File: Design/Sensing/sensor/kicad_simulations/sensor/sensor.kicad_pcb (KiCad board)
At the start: 2 copper layers, 41 parts, among them J1 Conn_01x14_Pin, J10 Conn_01x02_Pin, J11 Conn_01x01_Pin, J12 Conn_01x02_Pin, J13 Conn_01x02_Pin, J14 Conn_01x02_Pin, J15 Conn_01x02_Pin, J16 Conn_01x01_Pin, J17 Conn_01x02_Pin, J2 Conn_01x14_Pin, J3 Conn_01x02_Pin, J4 Conn_01x02_Pin, J5 Conn_01x02_Pin, J6 Conn_01x01_Pin, J7 Conn_01x02_Pin, J8 Conn_01x02_Pin, J9 Conn_01x02_Pin, Q1 2N3904, Q2 2N3904, Q3 2N3904, U1 TSSP58038, U2 TSSP58038, U3 TSSP58038, U4 BUF602xD, U5 BUF602xD, U6 BUF602xD

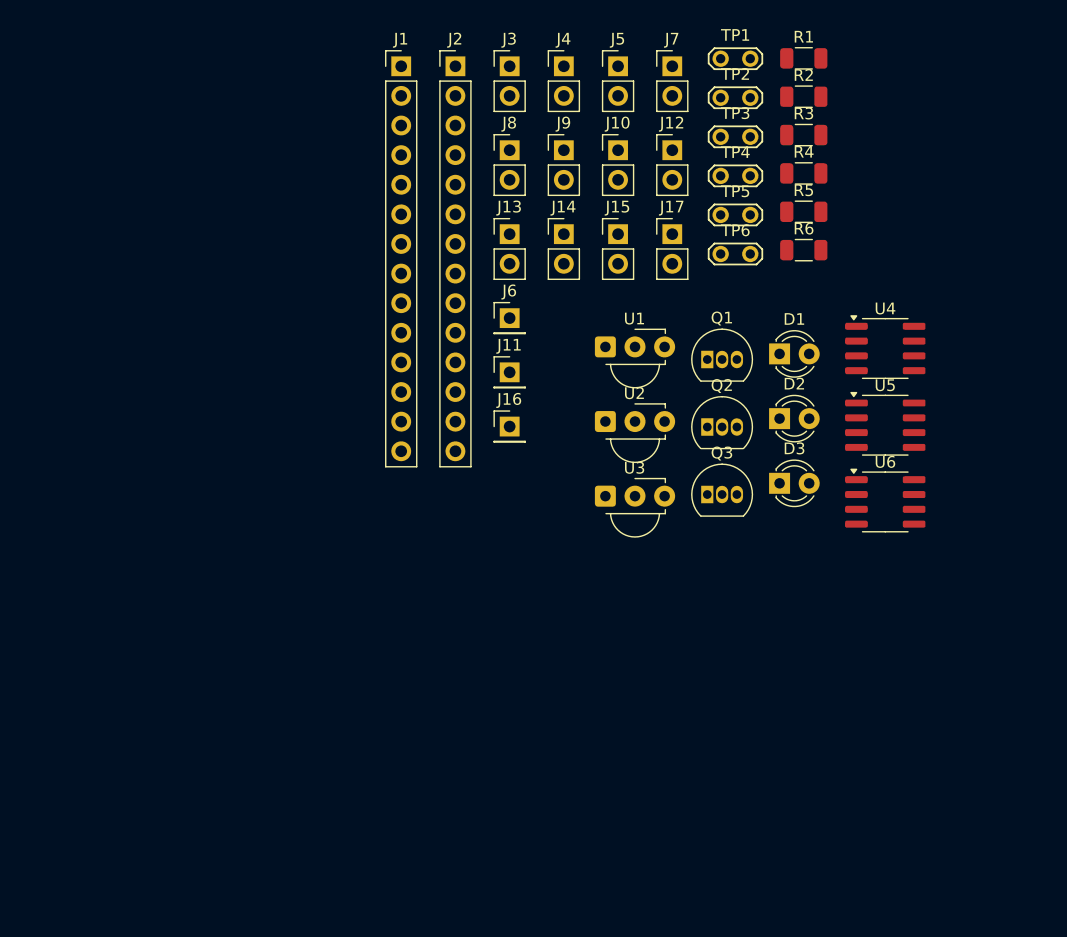
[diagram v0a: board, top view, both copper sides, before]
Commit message: PCB components placed but unrooted
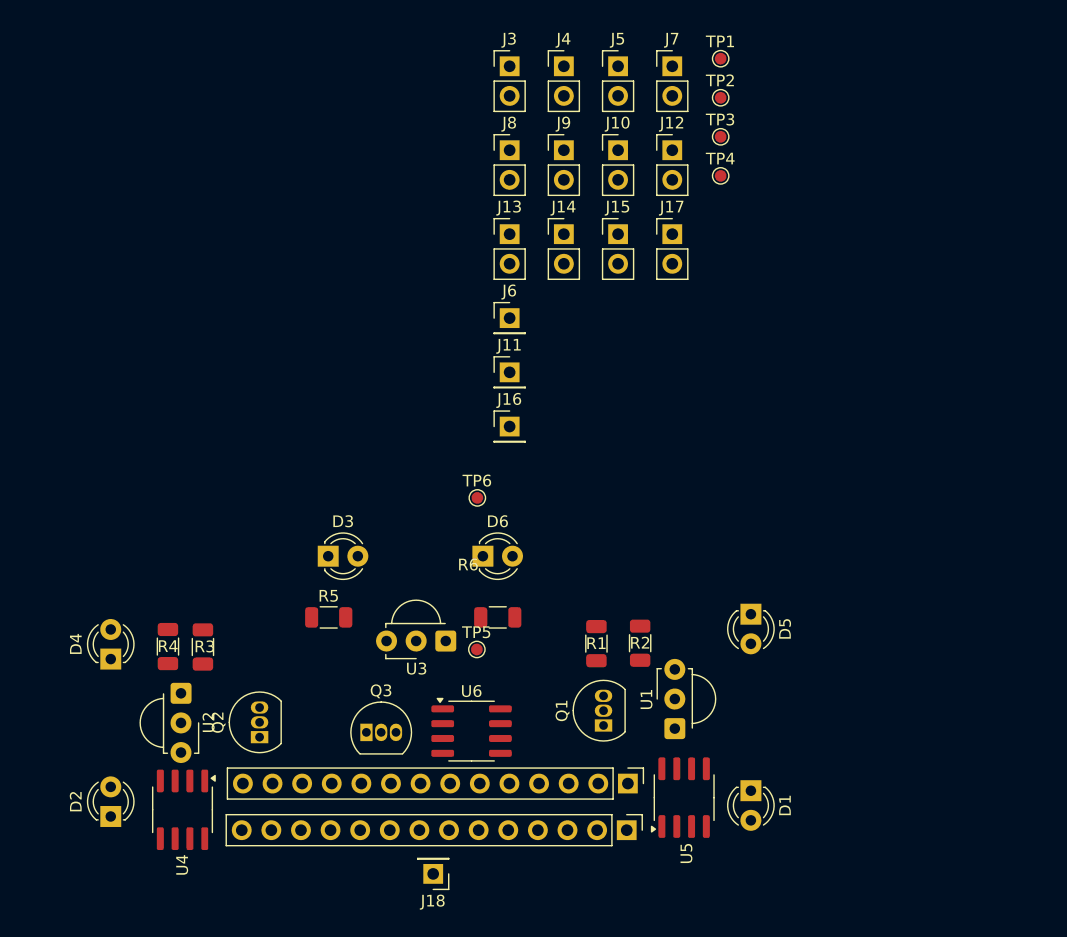
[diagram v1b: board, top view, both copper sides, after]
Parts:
- added D4: TSAL4400, LED_THT:LED_D3.0mm_IRBlack, F.Cu at (90.6, 108.6)
- added D5: TSAL4400, LED_THT:LED_D3.0mm_IRBlack, F.Cu at (145.5, 104.7)
- added D6: TSAL4400, LED_THT:LED_D3.0mm_IRBlack, F.Cu at (122.5, 99.8)
- added J18: Conn_01x01_Pin, Connector_PinHeader_2.54mm:PinHeader_1x01_P2.54mm_Vertical, F.Cu at (118.2, 127.0)
- TP1, TP2, TP3, TP4, TP5, TP6: footprint TestPoint:TestPoint_2Pads_Pitch2.54mm_Drill0.8mm -> TestPoint:TestPoint_Pad_D1.0mm
- moved U4 72.1 mm to (96.8, 121.5), turned to -90 degrees
- moved R4 68.0 mm to (95.5, 107.5), turned to 90 degrees
- moved R3 67.7 mm to (98.5, 107.5), turned to 90 degrees
- moved J2 67.1 mm to (134.8, 123.2), turned to -90 degrees
- moved D2 66.7 mm to (90.6, 122.1), turned to 90 degrees
- moved J1 64.5 mm to (134.9, 119.2), turned to -90 degrees
- moved R5 53.6 mm to (109.3, 105.0)
- moved R1 53.3 mm to (132.2, 107.2), turned to 90 degrees
- moved R2 48.9 mm to (136.0, 107.2), turned to 90 degrees
- moved Q2 46.7 mm to (103.4, 115.3), turned to 90 degrees
- moved U2 43.2 mm to (96.6, 111.5), turned to -90 degrees
- moved TP5 42.7 mm to (122.0, 107.8)
- moved R6 41.0 mm to (123.8, 105.0)
- moved U6 40.6 mm to (121.5, 114.8)
- moved D3 39.2 mm to (109.2, 99.8)
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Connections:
- D1 pad 2: /3V3 -> /5V
- D2 pad 2: /3V3 -> Net-(D2-A)
- D3 pad 2: /3V3 -> /5V
- J14 pad 1: /3V3 -> /5V
- J3 pad 1: /3V3 -> /5V
- J8 pad 1: /3V3 -> /5V
- R2 pad 2: Net-(D1-K) -> Net-(D5-K)
- R6 pad 2: Net-(D3-K) -> Net-(D6-K)

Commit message: working on pcb
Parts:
- removed J2: Conn_01x14_Pin, Connector_PinHeader_2.54mm:PinHeader_1x14_P2.54mm_Vertical
- J1: value Conn_01x14_Pin -> Conn_02x14_Counter_Clockwise; footprint Connector_PinHeader_2.54mm:PinHeader_1x14_P2.54mm_Vertical -> Connector_PinSocket_2.54mm:PinSocket_2x14_P2.54mm_Vertical
- moved J9 62.2 mm to (90.5, 113.5)
- moved J8 61.8 mm to (86.5, 113.5)
- moved J3 57.6 mm to (145.5, 111.5)
- moved J4 57.6 mm to (150.2, 111.5)
- moved J1 33.0 mm to (102.0, 120.5), turned to 90 degrees
- moved J11 25.6 mm to (103.5, 98.3)
- moved J13 25.6 mm to (103.5, 86.5)
- moved J14 25.6 mm to (108.2, 86.5)
- moved J16 25.6 mm to (103.5, 103.0)
- moved J6 25.6 mm to (103.5, 93.7)
- moved J5 25.6 mm to (112.8, 72.1)
- moved J7 25.6 mm to (117.5, 72.1)
- moved TP2 25.6 mm to (121.7, 74.8)
- moved J10 25.6 mm to (112.8, 79.3)
- moved J12 25.6 mm to (117.5, 79.3)
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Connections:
- J1 pad 10: /PE14 -> /PE9
- J1 pad 11: /PE15 -> /PE8
- J1 pad 12: /RESV2 -> /RESV1
- J1 pad 3: /RESV1 -> /RESV2
- J1 pad 4: /PE8 -> /PE15
- J1 pad 5: /PE9 -> /PE14
- J1 pad 6: /PA10 -> /PA13
- J1 pad 7: /PE11 -> /PE12
- J1 pad 8: /PE12 -> /PE11
- J1 pad 9: /PA13 -> /PA10

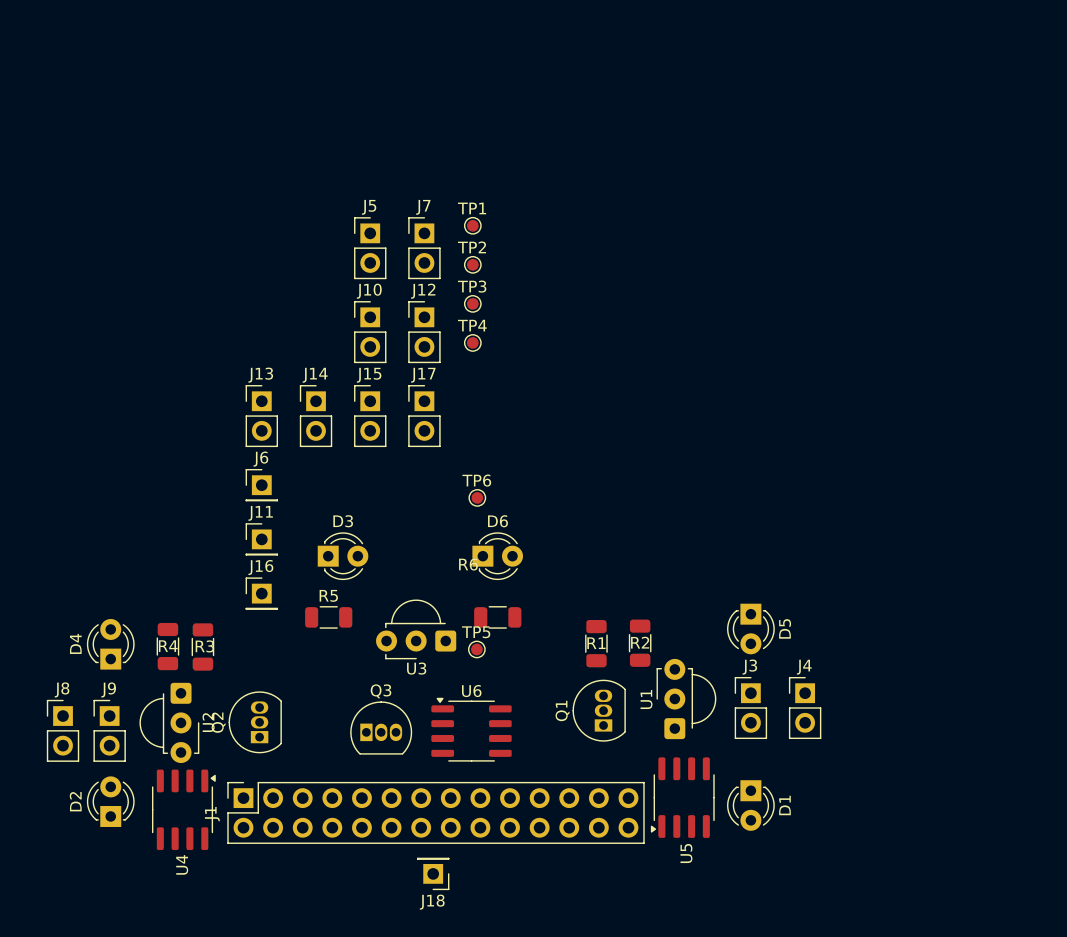
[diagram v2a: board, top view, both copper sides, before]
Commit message: PCB placement done, now need to root/make track connections
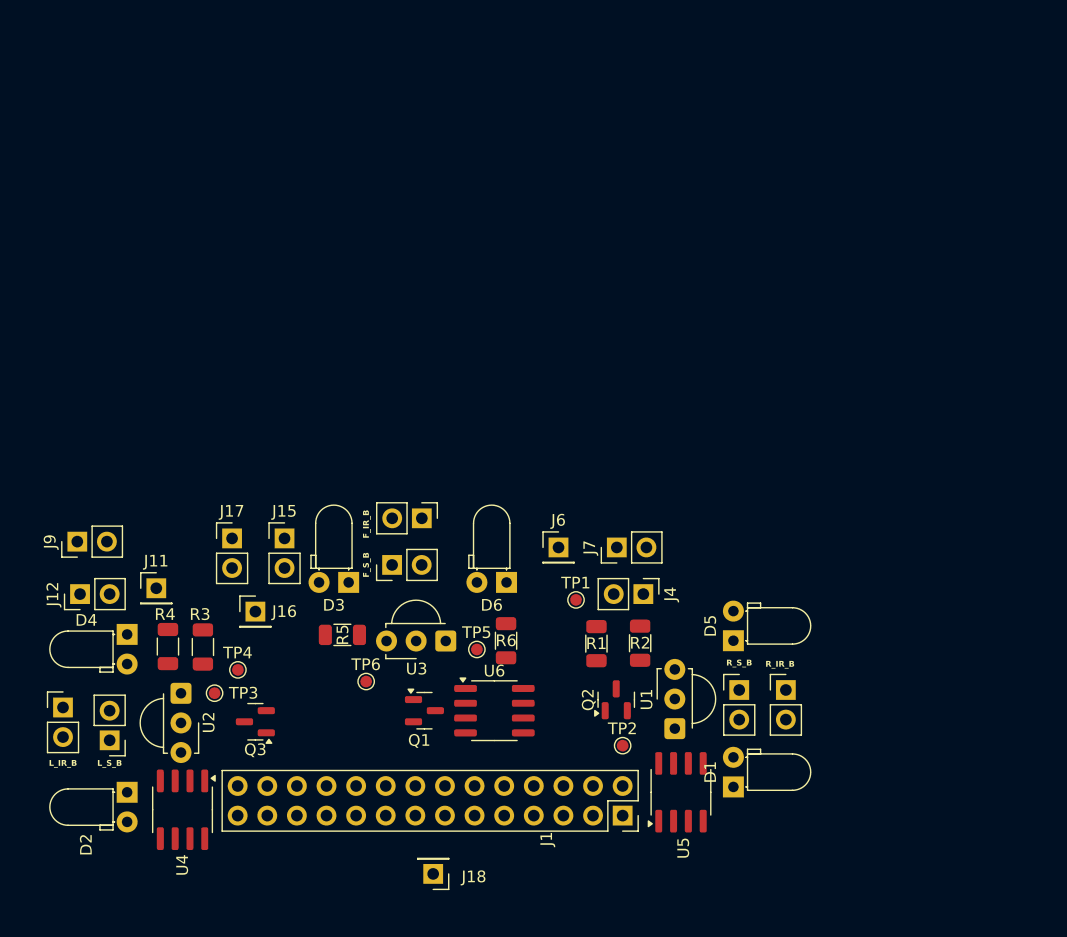
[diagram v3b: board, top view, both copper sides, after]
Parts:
- D1, D2, D3, D4, D5, D6: footprint LED_THT:LED_D3.0mm_IRBlack -> LED_THT:LED_D3.0mm_Horizontal_O1.27mm_Z2.0mm_IRBlack
- Q1, Q2, Q3: value 2N3904 -> MMBT2222A; footprint Package_TO_SOT_THT:TO-92_Inline -> Package_TO_SOT_SMD:SOT-23
- moved R_S_B 50.4 mm to (144.5, 111.2)
- moved TP2 43.2 mm to (134.5, 116.0)
- moved L_S_B 42.6 mm to (90.5, 115.5), turned to 180 degrees
- moved TP3 40.1 mm to (99.5, 111.5)
- moved J12 37.9 mm to (88.0, 103.0), turned to 90 degrees
- moved TP4 34.5 mm to (101.5, 109.5)
- moved TP1 33.3 mm to (130.5, 103.5)
- moved J1 32.6 mm to (134.5, 122.0), turned to -90 degrees
- moved J7 31.6 mm to (134.0, 99.0), turned to 90 degrees
- moved Q2 30.8 mm to (133.9, 112.1)
- moved J6 26.0 mm to (129.0, 99.0)
- moved J17 20.3 mm to (101.0, 98.2)
- moved TP6 18.4 mm to (112.5, 110.5)
- moved F_S_B 17.9 mm to (114.7, 100.5), turned to 90 degrees
- moved J4 16.3 mm to (136.3, 103.0), turned to -90 degrees
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- renumbered J14 to F_IR_B, J13 to F_S_B, J8 to L_IR_B, J10 to L_S_B, J3 to R_IR_B, J5 to R_S_B
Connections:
- J1 pad 1: /3V3 -> /RESV3
- J1 pad 10: /PE9 -> /PC4
- J1 pad 11: /PE8 -> GND
- J1 pad 12: /RESV1 -> /PC5
- J1 pad 13: /BATT -> /AB0
- J1 pad 14: /3V3 -> GND
- J1 pad 15: GND -> /3V3
- J1 pad 16: /AB0 -> /BATT
- J1 pad 17: /PC5 -> /RESV2
- J1 pad 18: GND -> /PE15
- J1 pad 19: /PC4 -> /PE14
- J1 pad 2: /BATT -> GND
- J1 pad 20: /PA7 -> /PA13
- J1 pad 21: GND -> /PE12
- J1 pad 22: /PA6 -> /PE11
- J1 pad 23: /PA5 -> /PA10
- J1 pad 24: GND -> /PE9
- J1 pad 25: /PA4 -> /PE8
- J1 pad 26: /PA3 -> /RESV1
- J1 pad 27: GND -> /BATT
- J1 pad 28: /RESV3 -> /3V3
- J1 pad 3: /RESV2 -> /PA3
- J1 pad 4: /PE15 -> /PA4
- J1 pad 5: /PE14 -> GND
- J1 pad 6: /PA13 -> /PA5
- J1 pad 7: /PE12 -> /PA6
- J1 pad 8: /PE11 -> GND
- J1 pad 9: /PA10 -> /PA7
- Q1 pad 1: GND -> Net-(Q1-B)
- Q1 pad 2: Net-(Q1-B) -> GND
- Q1 pad 3: Net-(J4-Pin_2) -> Net-(J15-Pin_2)
- Q2 pad 1: GND -> Net-(Q2-B)
- Q2 pad 2: Net-(Q2-B) -> GND
- Q2 pad 3: Net-(J9-Pin_2) -> Net-(J4-Pin_2)
- Q3 pad 1: GND -> Net-(Q3-B)
- Q3 pad 2: Net-(Q3-B) -> GND
- Q3 pad 3: Net-(J15-Pin_2) -> Net-(J9-Pin_2)
- R1 pad 1: Net-(Q1-B) -> Net-(Q2-B)
- R1 pad 2: /PA4 -> /PE15
- R3 pad 1: Net-(Q2-B) -> Net-(Q3-B)
- R3 pad 2: /PA5 -> /PE15
- R5 pad 1: Net-(Q3-B) -> Net-(Q1-B)
- R5 pad 2: /PA3 -> /PE15

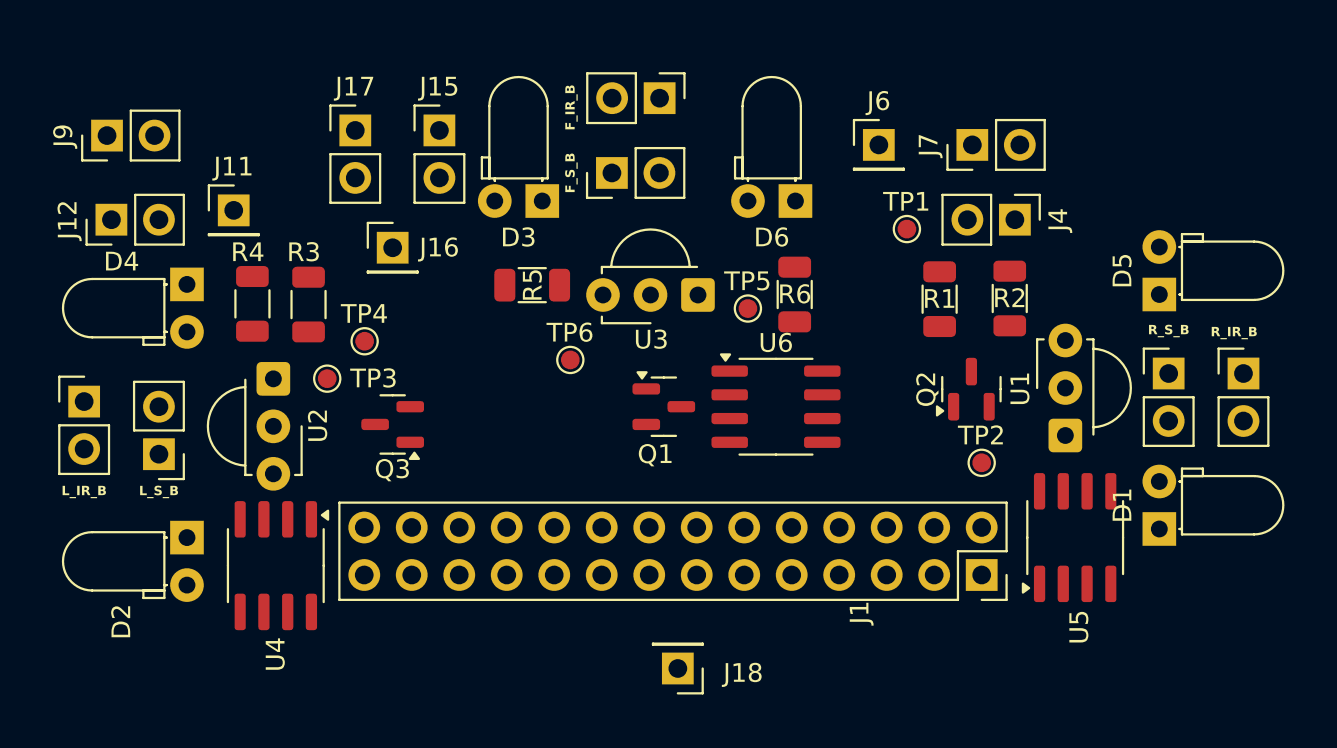
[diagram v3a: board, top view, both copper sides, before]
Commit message: PCB track done but still have 23 unrouted
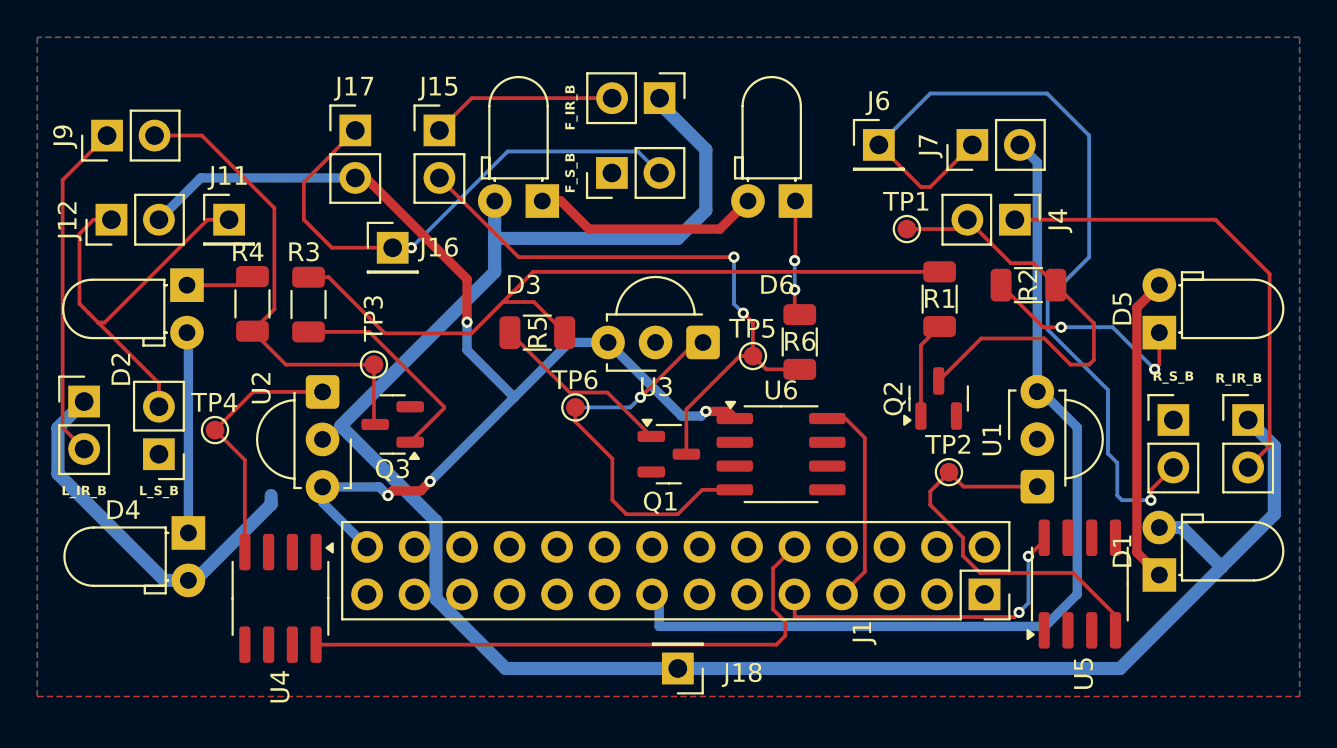
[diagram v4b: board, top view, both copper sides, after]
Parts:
- moved D2 13.5 mm to (92.0, 106.5)
- moved D4 13.3 mm to (92.1, 119.8)
- moved TP4 9.30 mm to (93.5, 114.2)
- moved U1 3.12 mm to (137.5, 117.3)
- moved U2 2.72 mm to (99.2, 112.2)
- moved TP3 2.61 mm to (102.0, 110.8), turned to 90 degrees
- moved Q1 2.55 mm to (117.8, 115.5)
- moved R5 2.55 mm to (110.7, 109.0)
- moved R6 2.55 mm to (124.8, 109.5)
- moved TP5 2.55 mm to (122.3, 110.3)
- moved TP6 2.55 mm to (112.8, 113.0)
- moved U6 2.55 mm to (123.8, 115.5)
- moved U3 2.55 mm to (119.6, 109.6)
- moved R_IR_B 2.50 mm to (148.8, 113.7)
- moved R_S_B 2.50 mm to (144.8, 113.7)
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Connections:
- J1 pad 23: /PA10 -> /5V
- J1 pad 25: /PE8 -> /5V
- J1 pad 26: /RESV1 -> /5V
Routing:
- net /5V: track 0.00 -> 125.7 mm
- net /3V3: track 0.00 -> 109.1 mm, vias 0 -> 4
- net Net-(J5-Pin_2): track 0.00 -> 46.1 mm, vias 0 -> 1
- net /PE15: track 0.00 -> 40.3 mm
- net Net-(J15-Pin_2): track 0.00 -> 33.2 mm, vias 0 -> 2
- net /PC4: track 0.00 -> 30.8 mm
- net Net-(J13-Pin_2): track 0.00 -> 28.2 mm, vias 0 -> 1
- net Net-(J3-Pin_2): track 0.00 -> 25.7 mm
- net Net-(J9-Pin_2): track 0.00 -> 25.6 mm
- net Net-(J4-Pin_2): track 0.00 -> 24.4 mm
- net Net-(J10-Pin_2): track 0.00 -> 22.3 mm
- net Net-(U3-OUT): track 0.00 -> 21.4 mm, vias 0 -> 1
- net Net-(U1-OUT): track 0.00 -> 20.9 mm
- net Net-(J8-Pin_2): track 0.00 -> 18.2 mm
- net /PA7: track 0.00 -> 17.9 mm, vias 0 -> 2
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- added copper zone on B.Cu, net GND
- added copper zone on F.Cu, net GND
